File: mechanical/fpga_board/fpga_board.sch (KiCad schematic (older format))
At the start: 36 parts, among them J1 Conn_02x17_Odd_Even, J2 Conn_02x17_Odd_Even, J3 Conn_02x17_Odd_Even, J4 Conn_02x17_Odd_Even, J5 Conn_02x17_Odd_Even, J6 jtag, J7 Conn_02x03_Odd_Even, U1 XC6SLX16-FTG256

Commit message: all fpga pins routed, still need regulators
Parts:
- added J8: Conn_02x12_Odd_Even, Connector_PinSocket_2.54mm:PinSocket_2x11_P2.54mm_Vertical, symbol Connector_Generic:Conn_02x11_Odd_Even
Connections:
- net T1+1: now also U1.M13 (IO_L74P_AWAKE_1)
- net T1+3: now also U1.B3 (IO_L83P_3)
- net T1+4: now also U1.M11 (IO_L2N_CMPMOSI_2)
- net T1+5: now also U1.M15 (IO_L46P_FCS_B_M1DQ2_1)
- net T1-1: now also U1.G14 (IO_L36P_A9_M1BA0_1)
- net T1-3: now also U1.C6 (IO_L7N_0)
- net T1-4: now also U1.T4 (IO_L63N_2)
- net T1-5: now also U1.R15 (IO_L49P_M1DQ10_1)
- net T10+1: now also U1.F14 (IO_L32N_A16_M1A9_1)
- net T10+3: now also U1.B14 (IO_L65P_SCP3_0)
- net T10+4: now also U1.R1 (IO_L32N_M3DQ15_3)
- net T10+5: now also U1.R12 (IO_L52P_M1DQ14_1)
- net T10-1: now also U1.C16 (IO_L33N_A14_M1A4_1); no longer U1.B3 (IO_L83P_3)
- net T10-3: now also U1.D11 (IO_L66P_SCP1_0)
- net T10-4: now also U1.L1 (IO_L36N_M3DQ9_3)
- net T10-5: now also U1.T6 (IO_L47N_2)
- net T11+1: now also U1.H15 (IO_L37P_A7_M1A0_1)
- net T11+3: now also U1.A12 (IO_L62N_VREF_0)
- net T11+4: now also U1.K5 (IO_L47P_M3A0_3)
- net T11+5: now also U1.P7 (IO_L31P_GCLK31_D14_2)
- net T11-1: now also U1.E12 (IO_L1N_A24_VREF_1); no longer U1.C3 (IO_L48P_M3BA0_3)
- net T11-3: now also U1.C11 (IO_L39P_0)
- net T11-4: now also U1.M1 (IO_L35N_M3DQ11_3)
- net T11-5: now also U1.T7 (IO_L32N_GCLK28_2)
- net T12+1: now also U1.H14 (IO_L39N_M1ODT_1)
- net T12+3: now also U1.A11 (IO_L39N_0)
- net T12+4: now also U1.L5 (IO_L45N_M3ODT_3)
- net T12+5: now also U1.N8 (IO_L29N_GCLK2_2)
- net T12-1: now also U1.E15 (IO_L34P_A13_M1WE_1)
- net T12-3: now also U1.D9 (IO_L40N_0)
- net T12-4: now also U1.N1 (IO_L34N_M3UDQSN_3)
- net T12-5: now also U1.T8 (IO_L30N_GCLK0_USERCCLK_2)
- net T13+1: now also U1.F16 (IO_L35N_A10_M1A2_1)
- net T13+3: now also U1.A13 (IO_L63N_SCP6_0)
- net T13+4: now also U1.P2 (IO_L33P_M3DQ12_3)
- net T13+5: now also U1.T10 (IO_L3N_MOSI_CSI_B_MISO0_2)
- net T13-1: now also U1.C15 (IO_L33P_A15_M1A10_1); no longer U1.A3 (IO_L83N_VREF_3)
- net T13-3: now also U1.E11 (IO_L64N_SCP4_0)
- net T13-4: now also U1.K2 (IO_L37P_M3DQ0_3)
- net T13-5: now also U1.R5 (IO_L48P_D7_2)
- net T14+1: now also U1.G16 (IO_L36N_A8_M1BA1_1)
- net T14+3: now also U1.B12 (IO_L62P_0)
- net T14+4: now also U1.R2 (IO_L32P_M3DQ14_3)
- net T14+5: now also U1.N6 (IO_L64N_D9_2)
- net T14-1: now also U1.D14 (IO_L31P_A19_M1CKE_1); no longer U1.A4 (IO_L1N_VREF_0)
- net T14-3: now also U1.E10 (IO_L37P_GCLK13_0)
- net T14-4: now also U1.L3 (IO_L36P_M3DQ8_3)
- net T14-5: now also U1.R7 (IO_L32P_GCLK29_2)
- net T15+1: now also U1.H16 (IO_L37N_A6_M1A1_1)
- net T15+3: now also U1.C10 (IO_L37N_GCLK12_0)
- net T15+4: now also U1.M4 (IO_L1P_3)
- net T15+5: now also U1.M9 (IO_L29P_GCLK3_2)
- net T15-1: now also U1.D16 (IO_L31N_A18_M1A12_1)
- net T15-3: now also U1.C9 (IO_L34P_GCLK19_0)
- net T15-4: now also U1.M2 (IO_L35P_M3DQ10_3)
- net T15-5: now also U1.P8 (IO_L30P_GCLK1_D13_2)
- net T16+1: now also U1.J16 (IO_L43N_GCLK4_M1DQ5_1)
- net T16+3: now also U1.A10 (IO_L35N_GCLK16_0)
- net T16+4: now also U1.M3 (IO_L1N_VREF_3)
- net T16+5: now also U1.P9 (IO_L14N_D12_2)
- net T16-1: now also U1.E16 (IO_L34N_A12_M1BA2_1)
- net T16-3: now also U1.A14 (IO_L65N_SCP2_0)
- net T16-4: now also U1.N3 (IO_L34P_M3UDQS_3)
- net T16-5: now also U1.R9 (IO_L23P_2)
- net T2+1: now also U1.L14 (IO_L47P_FWE_B_M1DQ0_1)
- net T2+3: now also U1.C3 (IO_L48P_M3BA0_3)
- net T2+4: now also U1.L10 (IO_L16P_2)
- net T2+5: now also U1.M14 (IO_L74N_DOUT_BUSY_1)
- net T2-1: now also U1.E13 (IO_L1P_A25_1)
- net T2-3: now also U1.B8 (IO_L33P_0)
- net T2-4: now also U1.P6 (IO_L47P_2)
- net T2-5: now also U1.R14 (IO_L50P_M1UDQS_1)
- net T3+1: now also U1.K12 (IO_L42P_GCLK7_M1UDM_1)
- net T3+3: now also U1.B5 (IO_L2P_0)
- net T3+4: now also U1.L8 (IO_L62P_D5_2)
- net T3+5: now also U1.P15 (IO_L48P_HDC_M1DQ8_1)
- net T3-1: now also U1.K14 (IO_L41N_GCLK8_M1CASN_1)
- net T3-3: now also U1.C8 (IO_L38N_VREF_0)
- net T3-4: now also U1.T3 (IO_L65N_CSO_B_2)
- net T3-5: now also U1.N12 (IO_L12P_D1_MISO2_2)
- net T4+1: now also U1.J13 (IO_L41P_GCLK9_IRDY1_M1RASN_1)
- net T4+3: now also U1.B6 (IO_L4P_0)
- net T4+4: now also U1.L7 (IO_L62N_D6_2)
- net T4+5: now also U1.R16 (IO_L49N_M1DQ11_1)
- net T4-1: now also U1.K15 (IO_L44P_A3_M1DQ6_1)
- net T4-3: now also U1.B10 (IO_L35P_GCLK17_0)
- net T4-4: now also U1.M5 (IO_L2P_3)
- net T4-5: now also U1.P12 (IO_L12N_D2_MISO3_2)
- net T5+1: now also U1.N14 (IO_L45P_A1_M1LDQS_1)
- net T5+3: now also U1.A2 (IO_L52N_M3A9_3)
- net T5+4: now also U1.M12 (IO_L2P_CMPCLK_2)
- net T5+5: now also U1.M16 (IO_L46N_FOE_B_M1DQ3_1)
- net T5-1: now also U1.J12 (IO_L40N_GCLK10_M1A6_1)
- net T5-3: now also U1.A6 (IO_L4N_0)
- net T5-4: now also U1.N5 (IO_L49P_D3_2)
- net T5-5: now also U1.T14 (IO_L51P_M1DQ12_1)
- net T6+1: now also U1.L12 (IO_L53P_1)
- net T6+3: now also U1.A3 (IO_L83N_VREF_3)
- net T6+4: now also U1.M10 (IO_L16N_VREF_2)
- net T6+5: now also U1.N16 (IO_L45N_A0_M1LDQSN_1)
- net T6-1: now also U1.F13 (IO_L32P_A17_M1A8_1)
- net T6-3: now also U1.A7 (IO_L6N_0)
- net T6-4: now also U1.M6 (IO_L64P_D8_2)
- net T6-5: now also U1.T13 (IO_L51N_M1DQ13_1)
- net T7+1: now also U1.L13 (IO_L53N_VREF_1)
- net T7+3: now also U1.A4 (IO_L1N_VREF_0)
- net T7+4: now also U1.M7 (IO_L31N_GCLK30_D15_2)
- net T7+5: now also U1.P16 (IO_L48N_M1DQ9_1)
- net T7-1: now also U1.L16 (IO_L47N_LDC_M1DQ1_1)
- net T7-3: now also U1.A8 (IO_L33N_0)
- net T7-4: now also U1.P4 (IO_L63P_2)
- net T7-5: now also U1.P11 (IO_L13N_D10_2)
- net T8+1: now also U1.J14 (IO_L43P_GCLK5_M1DQ4_1)
- net T8+3: now also U1.A5 (IO_L2N_0)
- net T8+4: now also U1.P5 (IO_L49N_D4_2)
- net T8+5: now also U1.T15 (IO_L50N_M1UDQSN_1)
- net T8-1: now also U1.K16 (IO_L44N_A2_M1DQ7_1)
- net T8-3: now also U1.A9 (IO_L34N_GCLK18_0)
- net T8-4: now also U1.N4 (IO_L2N_3)
- net T8-5: now also U1.N9 (IO_L14P_D11_2)
- net T9+1: now also U1.F15 (IO_L35P_A11_M1A7_1)
- net T9+3: now also U1.B15 (IO_L29P_A23_M1A13_1)
- net T9+4: now also U1.P1 (IO_L33N_M3DQ13_3)
- net T9+5: now also U1.T9 (IO_L23N_2)
- net T9-1: now also U1.B16 (IO_L29N_A22_M1A14_1); no longer U1.A2 (IO_L52N_M3A9_3)
- net T9-3: now also U1.D12 (IO_L66N_SCP0_0)
- net T9-4: now also U1.K1 (IO_L37N_M3DQ1_3)
- net T9-5: now also U1.T5 (IO_L48N_RDWR_B_VREF_2)
- net gnd: now also J8.21 (Pin_21), J8.22 (Pin_22)
- net extra19: now reaches U1.C13 (IO_L63P_SCP7_0)
- net extra19: now also J8.19 (Pin_19)
- net extra5: now reaches U1.C5 (IO_L3N_0)
- net extra5: now also J8.5 (Pin_5)
- net extra9: now reaches U1.C7 (IO_L6P_0)
- net extra9: now also J8.9 (Pin_9)
- net extra1: now reaches U1.D5 (IO_L3P_0)
- net extra1: now also J8.1 (Pin_1)
- net extra7: now reaches U1.D6 (IO_L7P_0)
- net extra7: now also J8.7 (Pin_7)
- net extra11: now reaches U1.D8 (IO_L38P_0)
- net extra11: now also J8.11 (Pin_11)
- net extra3: now reaches U1.E6 (IO_L5N_0)
- net extra3: now also J8.3 (Pin_3)
- net extra4: now reaches U1.E7 (IO_L36P_GCLK15_0)
- net extra4: now also J8.4 (Pin_4)
- net extra8: now reaches U1.E8 (IO_L36N_GCLK14_0)
- net extra8: now also J8.8 (Pin_8)
- net extra10: now reaches U1.F10 (IO_L64P_SCP5_0)
- net extra10: now also J8.10 (Pin_10)
- net extra14: now reaches U1.F12 (IO_L30P_A21_M1RESET_1)
- net extra14: now also J8.14 (Pin_14)
- net extra2: now reaches U1.F7 (IO_L5P_0)
- net extra2: now also J8.2 (Pin_2)
- net extra12: now reaches U1.F9 (IO_L40P_0)
- net extra12: now also J8.12 (Pin_12)
- net extra6: now reaches U1.G11 (IO_L30N_A20_M1A11_1)
- net extra6: now also J8.6 (Pin_6)
- net extra16: now reaches U1.G12 (IO_L38P_A5_M1CLK_1)
- net extra16: now also J8.16 (Pin_16)
- net extra13: now reaches U1.H11 (IO_L38N_A4_M1CLKN_1)
- net extra13: now also J8.13 (Pin_13)
- net extra15: now reaches U1.H13 (IO_L39P_M1A3_1)
- net extra15: now also J8.15 (Pin_15)
- net extra17: now reaches U1.J11 (IO_L40P_GCLK11_M1A5_1)
- net extra17: now also J8.17 (Pin_17)
- net extra18: now reaches U1.K11 (IO_L42N_GCLK6_TRDY1_M1LDM_1)
- net extra18: now also J8.18 (Pin_18)
- net extra20: now reaches U1.T12 (IO_L52N_M1DQ15_1)
- net extra20: now also J8.20 (Pin_20)
- no-connect marks 10 -> 11
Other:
- moved on the sheet: J1, J3, J5

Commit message: constraint file extractor
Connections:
- net extra17: no longer U1.J11 (IO_L40P_GCLK11_M1A5_1)
- new net glckorsomething: U1.J11 (IO_L40P_GCLK11_M1A5_1)
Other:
- moved on the sheet: J1, J3, J4, J5

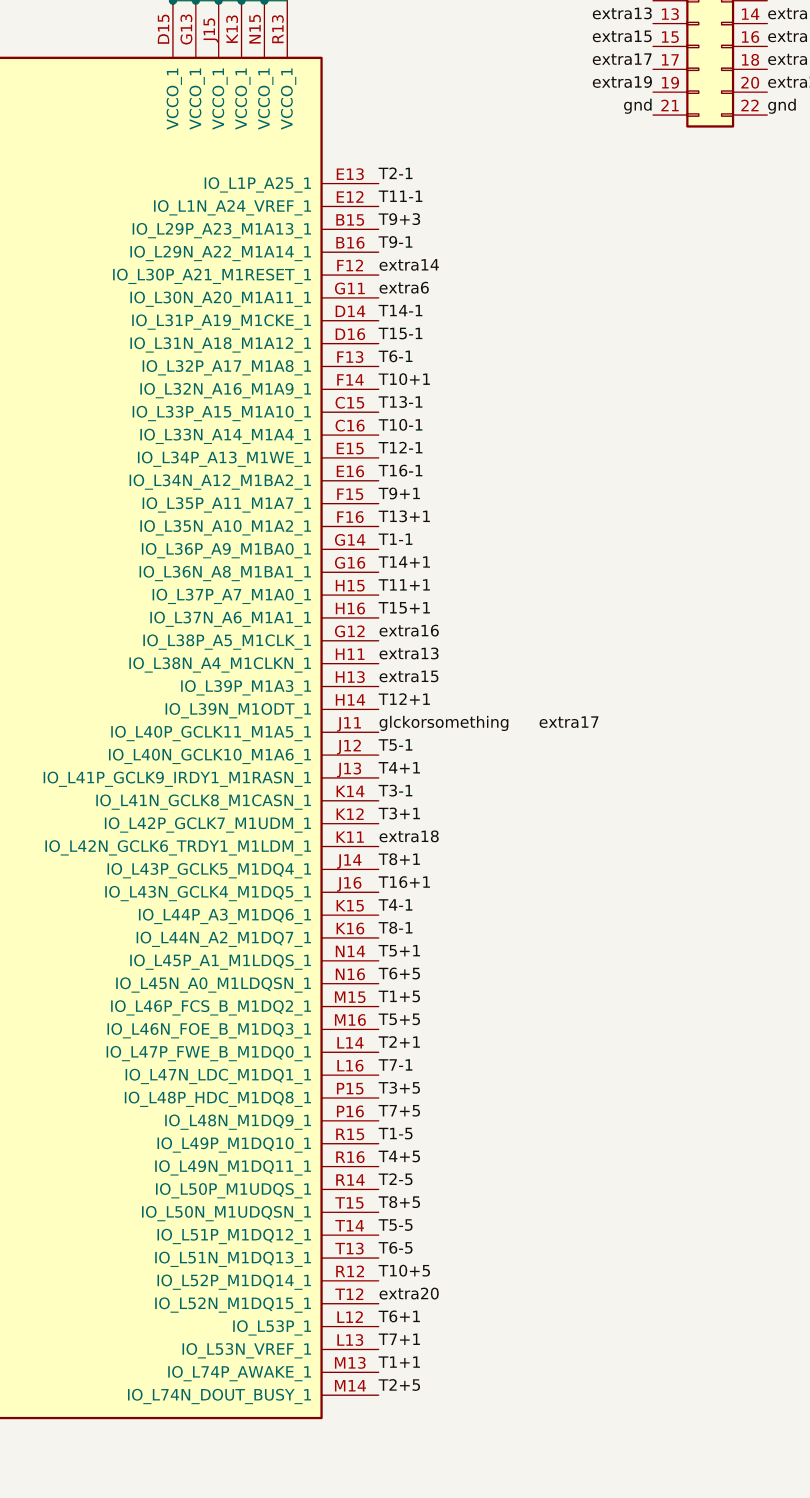
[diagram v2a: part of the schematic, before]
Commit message: Moved FPGA and added hole
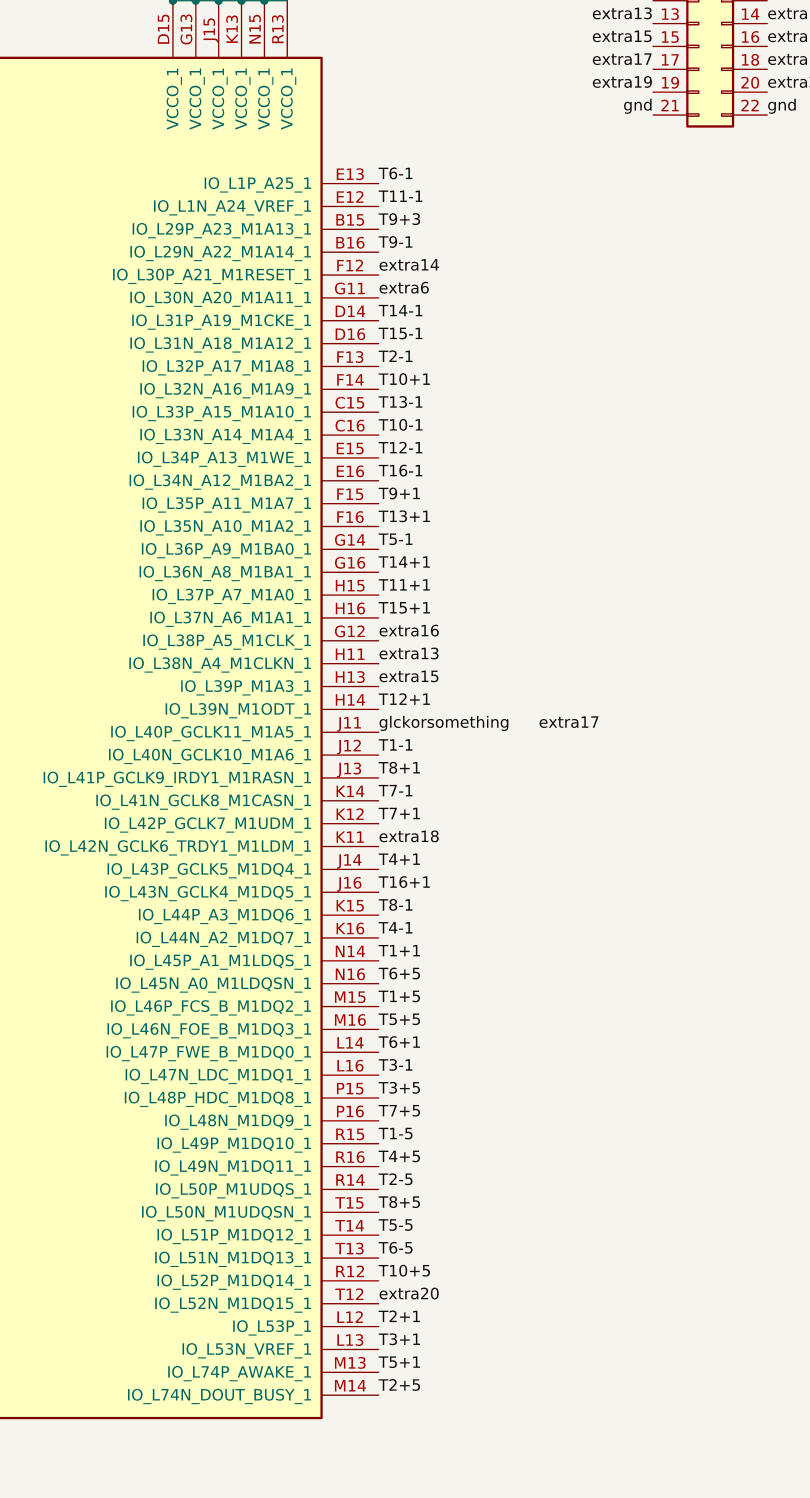
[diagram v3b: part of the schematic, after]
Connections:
- net T1+1: now also U1.N14 (IO_L45P_A1_M1LDQS_1); no longer U1.M13 (IO_L74P_AWAKE_1)
- net T1-1: now also U1.J12 (IO_L40N_GCLK10_M1A6_1); no longer U1.G14 (IO_L36P_A9_M1BA0_1)
- net T2+1: now also U1.L12 (IO_L53P_1); no longer U1.L14 (IO_L47P_FWE_B_M1DQ0_1)
- net T2-1: now also U1.F13 (IO_L32P_A17_M1A8_1); no longer U1.E13 (IO_L1P_A25_1)
- net T3+1: now also U1.L13 (IO_L53N_VREF_1); no longer U1.K12 (IO_L42P_GCLK7_M1UDM_1)
- net T3-1: now also U1.L16 (IO_L47N_LDC_M1DQ1_1); no longer U1.K14 (IO_L41N_GCLK8_M1CASN_1)
- net T4+1: now also U1.J14 (IO_L43P_GCLK5_M1DQ4_1); no longer U1.J13 (IO_L41P_GCLK9_IRDY1_M1RASN_1)
- net T4-1: now also U1.K16 (IO_L44N_A2_M1DQ7_1); no longer U1.K15 (IO_L44P_A3_M1DQ6_1)
- net T5+1: now also U1.M13 (IO_L74P_AWAKE_1); no longer U1.N14 (IO_L45P_A1_M1LDQS_1)
- net T5-1: now also U1.G14 (IO_L36P_A9_M1BA0_1); no longer U1.J12 (IO_L40N_GCLK10_M1A6_1)
- net T6+1: now also U1.L14 (IO_L47P_FWE_B_M1DQ0_1); no longer U1.L12 (IO_L53P_1)
- net T6-1: now also U1.E13 (IO_L1P_A25_1); no longer U1.F13 (IO_L32P_A17_M1A8_1)
- net T7+1: now also U1.K12 (IO_L42P_GCLK7_M1UDM_1); no longer U1.L13 (IO_L53N_VREF_1)
- net T7-1: now also U1.K14 (IO_L41N_GCLK8_M1CASN_1); no longer U1.L16 (IO_L47N_LDC_M1DQ1_1)
- net T8+1: now also U1.J13 (IO_L41P_GCLK9_IRDY1_M1RASN_1); no longer U1.J14 (IO_L43P_GCLK5_M1DQ4_1)
- net T8-1: now also U1.K15 (IO_L44P_A3_M1DQ6_1); no longer U1.K16 (IO_L44N_A2_M1DQ7_1)
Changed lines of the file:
@@
 T16+1
 Text Label 8850 10500 0    50   ~ 0
+T8-1
+Text Label 8850 10600 0    50   ~ 0
 T4-1
-Text Label 8850 10600 0    50   ~ 0
-T8-1
 Text Label 8850 10000 0    50   ~ 0
+T7-1
+Text Label 8850 11200 0    50   ~ 0
 T3-1
-Text Label 8850 11200 0    50   ~ 0
-T7-1
 Text Label 8850 7400 0    50   ~ 0
 T11-1
@@
 T14-1
 Text Label 8850 8100 0    50   ~ 0
+T2-1
+Text Label 8850 8900 0    50   ~ 0
+T5-1
+Text Label 8850 9800 0    50   ~ 0
+T1-1
+Text Label 8850 9900 0    50   ~ 0
+T8+1
+Text Label 8850 10300 0    50   ~ 0
+T4+1
+Text Label 8850 10100 0    50   ~ 0
+T7+1
+Text Label 8850 12400 0    50   ~ 0
+T3+1
+Text Label 8850 11100 0    50   ~ 0
+T6+1
+Text Label 8850 7300 0    50   ~ 0
 T6-1
-Text Label 8850 8900 0    50   ~ 0
-T1-1
-Text Label 8850 9800 0    50   ~ 0
-T5-1
-Text Label 8850 9900 0    50   ~ 0
-T4+1
-Text Label 8850 10300 0    50   ~ 0
-T8+1
-Text Label 8850 10100 0    50   ~ 0
-T3+1
-Text Label 8850 12400 0    50   ~ 0
-T7+1
-Text Label 8850 11100 0    50   ~ 0
+Text Label 8850 12300 0    50   ~ 0
 T2+1
-Text Label 8850 7300 0    50   ~ 0
-T2-1
-Text Label 8850 12300 0    50   ~ 0
-T6+1
 Text Label 8850 12500 0    50   ~ 0
+T5+1
+Text Label 8850 10700 0    50   ~ 0
 T1+1
-Text Label 8850 10700 0    50   ~ 0
-T5+1
 Text Label 4850 8900 2    50   ~ 0
 T15-3
